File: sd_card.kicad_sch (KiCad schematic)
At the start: 7 parts, among them J30 Micro_SD_Card

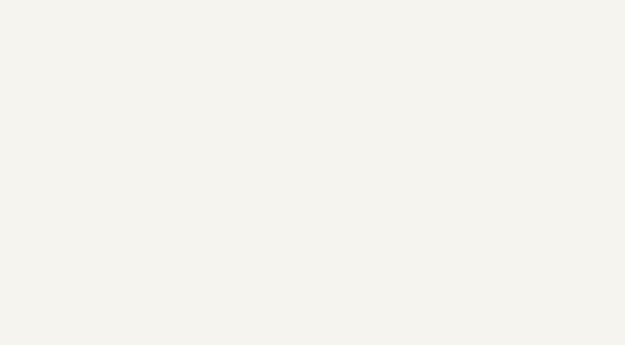
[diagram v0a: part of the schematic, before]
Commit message: Added schematic descriptions
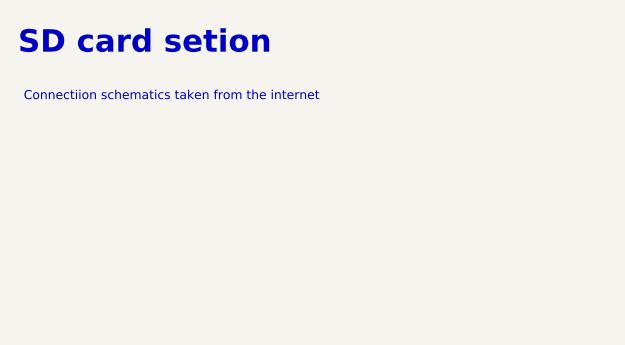
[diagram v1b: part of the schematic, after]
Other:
- note added: "Connectiion schematics taken from the internet"
- note added: "SD card setion"
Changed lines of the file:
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@@
   (title_block
     (title "Iron Warriors v2.0 ")
-    (date "2023-07-16")
+    (date "2023-08-01")
     (rev "1.1")
   )
@@
     (stroke (width 0) (type default) (color 0 0 0 0))
   )
+  (text "SD card setion\n" (at 19.685 20.32 0)
+    (effects (font (size 2.5 2.5) (thickness 0.254) bold) (justify left bottom))
+  )
+  (text "Connectiion schematics taken from the internet" (at 20.32 25.4 0)
+    (effects (font (size 1 1)) (justify left bottom))
+  )
   (global_label "sd_card_cs" (shape input) (at 132.08 91.44 180) (fields_autoplaced)
